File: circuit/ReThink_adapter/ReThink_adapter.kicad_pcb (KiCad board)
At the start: 2 copper layers, 82 x 52 mm, 82 parts, among them J1 FH34SRJ-34S-0.5SH(50), J10 OUT2, J11 OUT3, J2 FH34SRJ-6S-0.5SH(50), J3 Mezzanine, J4 XF3M(1)-3015-1B, J5 XF3M(1)-0815-1B, J6 FH34SRJ-40S-0.5SH(50), J7 FH52-40S-0.5SH, J8 XF3M(1)-1415-1B, J9 OUT1, U1 PCAL6416AHF, U2 LM2775DSG, U3 PCA9306, U4 TPS610333DRLR

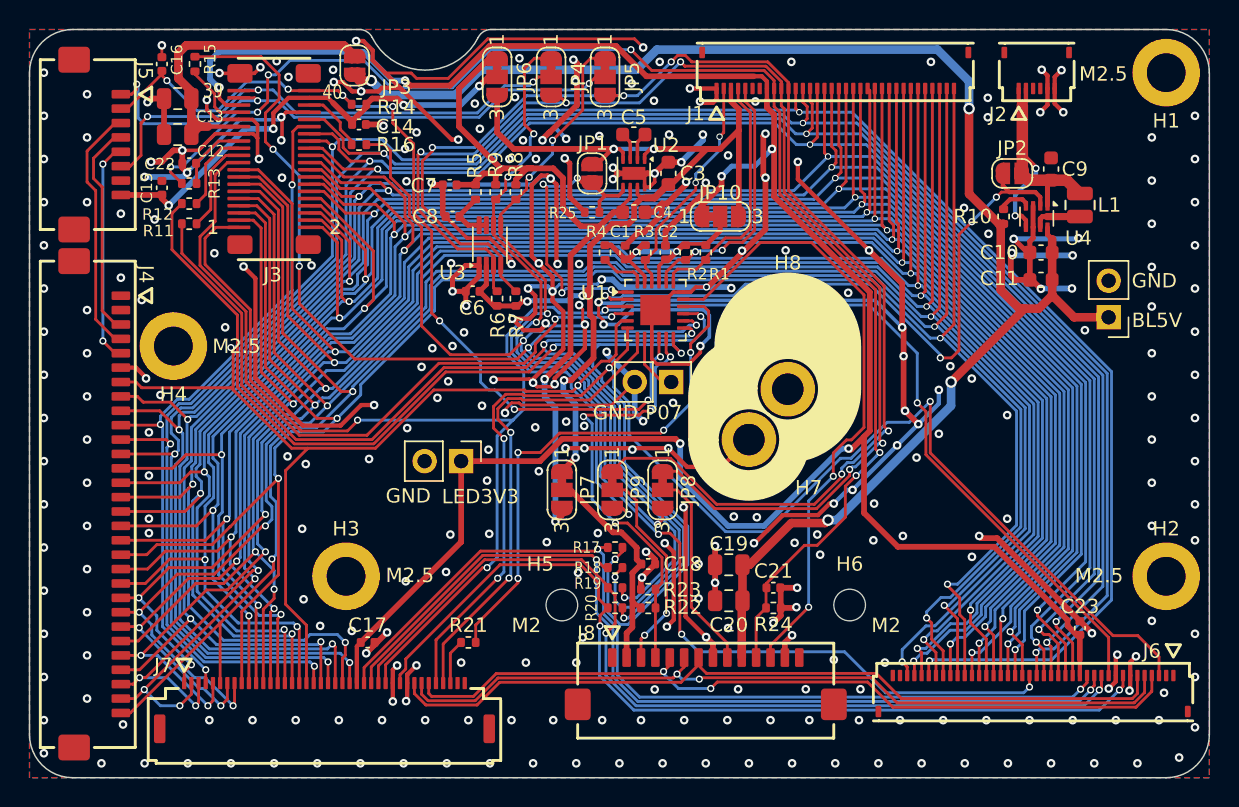
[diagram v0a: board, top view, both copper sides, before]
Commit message: add logo to PCB
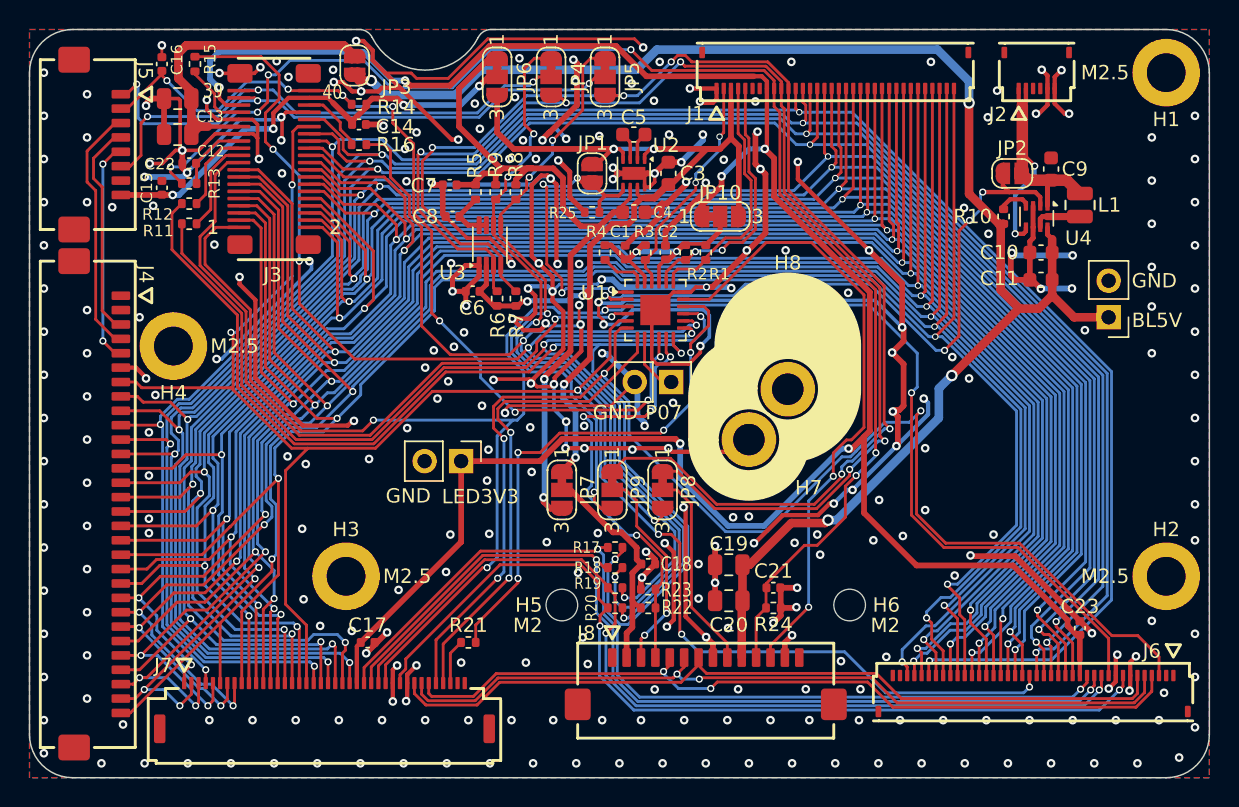
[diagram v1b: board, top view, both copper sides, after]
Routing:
- net GND: track 434.2 -> 447.9 mm, vias 320 -> 311
- net /HOTKEY: track 123.4 -> 126.9 mm
- net /DRV16: track 93.4 -> 95.6 mm
- net /LS_DAT: track 44.4 -> 42.6 mm
- net TP_3V3: track 75.3 -> 74.0 mm
- net TP_5V: track 54.0 -> 52.8 mm
- net VIN: track 20.4 -> 21.4 mm
- net TP1_PWR: track 33.2 -> 32.5 mm
- net /LS_CLK: track 44.4 -> 43.7 mm
- net /DRV5: track 141.0 -> 140.4 mm
- net /SENSE1: track 148.4 -> 147.8 mm
- net LED_3V3: track 162.7 -> 162.2 mm
